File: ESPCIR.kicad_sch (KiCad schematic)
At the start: 13 parts, among them J1 USB_C_Receptacle_USB2.0_16P, SW1 SW_MEC_5E, SW2 SW_MEC_5E, U1 ESP32-S3-WROOM-1, U3 AMS1117-3.3

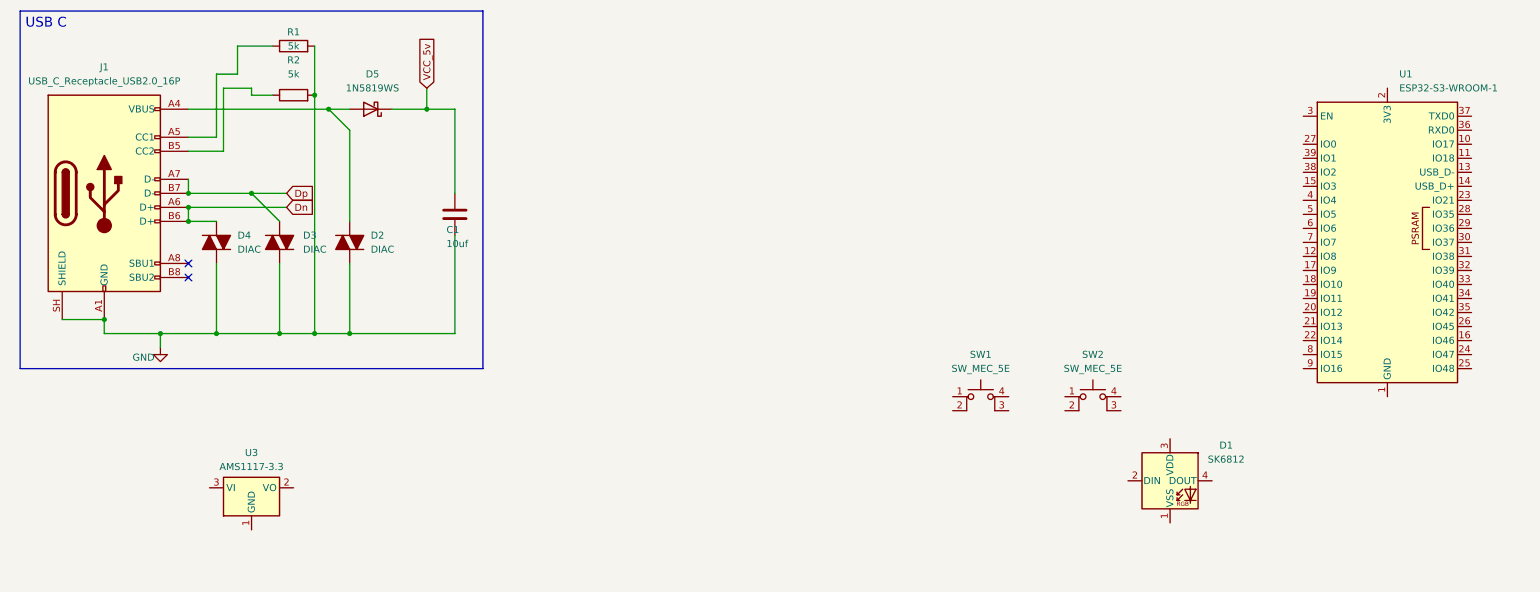
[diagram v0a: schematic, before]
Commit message: Wired the tft screen (Schem)
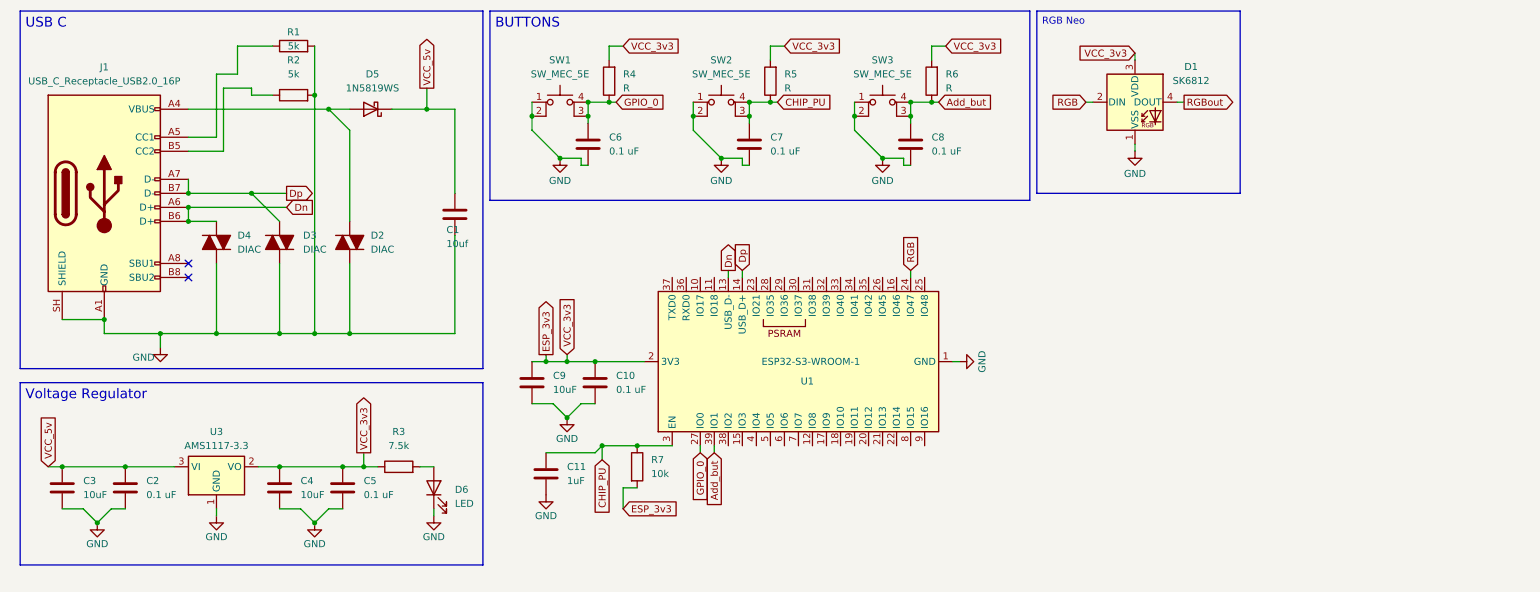
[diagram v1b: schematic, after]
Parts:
- added C10, C2, C5, C6, C7, C8: 0.1 uF, symbol Device:C
- added C11: 1uF, symbol Device:C
- added C3, C4, C9: 10uF, symbol Device:C
- added D6: LED, symbol Device:LED
- added R3: 7.5k, symbol Device:R
- added R4, R5, R6: R, symbol Device:R
- added R7: 10k, symbol Device:R
- added SW3: SW_MEC_5E, symbol Switch:SW_MEC_5E
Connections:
- net Dn: now also U1.13 (USB_D-)
- net Dp: now also U1.14 (USB_D+)
- net GND: now also D1.1 (VSS), SW1.1, SW1.2, SW2.1, SW2.2, U1.1 (GND), U1.40 (GND), U1.41 (GND), U3.1 (GND), C10.2, C11.2, C2.2, C3.2, C4.2, C5.2, C6.2, C7.2, C8.2, C9.2, D6.1 (K), SW3.1, SW3.2
- net VCC_5v: now also U3.3 (VI), C2.1, C3.1
- net CHIP_PU: now reaches SW2.3 (K)
- net CHIP_PU: now also SW2.4 (A), U1.3 (EN), C11.1, C7.1, R5.1, R7.1
- net GPIO_0: now reaches SW1.3 (K)
- net GPIO_0: now also SW1.4 (A), U1.27 (IO0), C6.1, R4.1
- net RGB: now reaches D1.2 (DIN)
- net RGB: now also U1.24 (IO47)
- net ESP_3v3: now reaches D1.3 (VDD)
- net ESP_3v3: now also U1.2 (3V3), U3.2 (VO), C10.1, C4.1, C5.1, C9.1, R3.1, R4.2, R5.2, R6.2, R7.2
- net RGBout: now reaches D1.4 (DOUT)
- net Add_but: now reaches U1.39 (IO1)
- net Add_but: now also C8.1, R6.1, SW3.3 (K), SW3.4 (A)
- new net: D6.2 (A), R3.2
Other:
- moved on the sheet: D1, SW1, U1, U3

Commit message: Assigned all the avaliable pins from the esp32 s3 gpio to labels (Schem)
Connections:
- net Add_but: now also U1.31 (IO38); no longer U1.39 (IO1)
- net TX: now reaches U1.10 (IO17)
- net RX: now reaches U1.11 (IO18)
- net SPI_CLK: now reaches U1.12 (IO8)
- net ADC1_IO3: now reaches U1.15 (IO3)
- net GPIO46: now reaches U1.16 (IO46)
- net SPI_MISO: now reaches U1.17 (IO9)
- net ANY_CS: now reaches U1.18 (IO10)
- net SPI2_MOIS: now reaches U1.19 (IO11)
- net SPI2_CLK: now reaches U1.20 (IO12)
- net SPI2_MISO: now reaches U1.21 (IO13)
- net TFT_CS: now reaches U1.22 (IO14)
- net GPIO21: now reaches U1.23 (IO21)
- net GPIO48: now reaches U1.25 (IO48)
- net GPIO45: now reaches U1.26 (IO45)
- net GPIO39: now reaches U1.32 (IO39)
- net GPIO40: now reaches U1.33 (IO40)
- net GPIO41: now reaches U1.34 (IO41)
- net GPIO42: now reaches U1.35 (IO42)
- net ADC1_IO2: now reaches U1.38 (IO2)
- net TFT_DC: now reaches U1.4 (IO4)
- net I2C_SDA: now reaches U1.5 (IO5)
- net I2C_SCL: now reaches U1.6 (IO6)
- net SPI_MOIS: now reaches U1.7 (IO7)
- net T_CS: now reaches U1.8 (IO15)
- net SD_CS: now reaches U1.9 (IO16)
- new net TFT_BL: U1.39 (IO1)
- no-connect marks 2 -> 7

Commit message: (Likely finished the Schem) Wired all the connectors and esp pins
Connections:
- net GPIO21 renamed T_IRQ
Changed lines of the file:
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@@
 			(font
 				(size 1.778 1.778)
+				(thickness 0.3556)
+				(bold yes)
+			)
+			(justify left top)
+		)
+	)
+	(text_box "ESP32-S3 Chip"
+		(exclude_from_sim no)
+		(at 97.79 49.53 0)
+		(size 92.71 66.04)
+		(margins 0.9525 0.9525 0.9525 0.9525)
+		(stroke
+			(width 0)
+			(type solid)
+		)
+		(fill
+			(type none)
+		)
+		(effects
+			(font
+				(size 1.27 1.27)
+				(thickness 0.254)
+				(bold yes)
 			)
 			(justify left top)
@@
 			(font
 				(size 1.27 1.27)
+				(thickness 0.254)
+				(bold yes)
 			)
 			(justify left top)
@@
 			(font
 				(size 1.778 1.778)
+				(thickness 0.3556)
+				(bold yes)
 			)
 			(justify left top)
@@
 			(font
 				(size 1.778 1.778)
+				(thickness 0.3556)
+				(bold yes)
 			)
 			(justify left top)
@@
 		)
 	)
-	(hierarchical_label "GPIO21"
-		(shape bidirectional)
+	(hierarchical_label "T_IRQ"
+		(shape input)
 		(at 146.05 59.69 90)
 		(effects

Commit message: Fully Finshed the schem
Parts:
- removed D2, D3, D4: DIAC, symbol Device:DIAC
- added D7, D8, D9: LESD5D5.0CT1G, Battery-extra:TVS_LESD5D5.0CT1G, symbol LESD5D5.0CT1G:LESD5D5.0CT1G
- C1, C10, C11, C2, C3, C4, C5, C6, C7, C8, C9: footprint (none) -> Capacitor_SMD:C_0603_1608Metric_Pad1.08x0.95mm_HandSolder
- D6: footprint (none) -> LED_SMD:LED_0603_1608Metric_Pad1.05x0.95mm_HandSolder
- J1: footprint (none) -> Connector_USB:USB_C_Receptacle_Amphenol_12401610E4-2A_CircularHoles
- R1, R2, R3, R7: footprint (none) -> Resistor_SMD:R_0603_1608Metric_Pad0.98x0.95mm_HandSolder
- R4, R5, R6: value R -> 10k; footprint (none) -> Resistor_SMD:R_0603_1608Metric_Pad0.98x0.95mm_HandSolder
- SW1, SW2, SW3: footprint (none) -> Button_Switch_SMD:SW_Push_1P1T_NO_CK_KMR2
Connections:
- net Dn: now also D7.2
- net Dp: now also D8.2
- net GND: now also D7.1, D8.1, D9.1
- net at D5.2 (A), J1.A4 (VBUS), J1.A9 (VBUS)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: now also D9.2
- net 0RX: now reaches U1.36 (RXD0)
- net 0TX: now reaches U1.37 (TXD0)
- no-connect marks 7 -> 5

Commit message: well placed all the compnents in their places (PCB)
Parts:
- SW1, SW2, SW3: footprint Button_Switch_SMD:SW_Push_1P1T_NO_CK_KMR2 -> RAM:SW_Push_1P1T_NO_CK_KMR2
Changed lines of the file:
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@@
 			)
 		)
-		(property "Footprint" "Button_Switch_SMD:SW_Push_1P1T_NO_CK_KMR2"
+		(property "Footprint" "RAM:SW_Push_1P1T_NO_CK_KMR2"
 			(at 110.49 24.13 0)
 			(hide yes)
@@
 			)
 		)
-		(property "Footprint" "Button_Switch_SMD:SW_Push_1P1T_NO_CK_KMR2"
+		(property "Footprint" "RAM:SW_Push_1P1T_NO_CK_KMR2"
 			(at 168.91 24.13 0)
 			(hide yes)
@@
 			)
 		)
-		(property "Footprint" "Button_Switch_SMD:SW_Push_1P1T_NO_CK_KMR2"
+		(property "Footprint" "RAM:SW_Push_1P1T_NO_CK_KMR2"
 			(at 139.7 24.13 0)
 			(hide yes)
